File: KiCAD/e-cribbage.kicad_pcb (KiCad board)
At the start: 2 copper layers, 304.8 x 100.3 mm, 568 parts, among them U1 74HC595D_118, U10 74HC595D_118, U11 74HC595D_118, U12 74HC595D_118, U13 74HC595D_118, U14 74HC595D_118, U15 74HC595D_118, U16 74HC595D_118, U17 74HC595D_118, U18 74HC595D_118, U19 74HC595D_118, U2 MSP430F2012IPW, U20 74HC595D_118, U21 74HC595D_118, U22 74HC595D_118, U23 74HC595D_118, U24 74HC595D_118, U25 74HC595D_118, U26 74HC595D_118, U27 74HC595D_118, U28 74HC595D_118, U29 74HC595D_118, U3 74HC595D_118, U30 74HC595D_118, U31 74HC595D_118, U32 SN74LVC1G08DBVR, U34 SN74LVC1G08DBVR, U35 SN74LVC1G08DBVR, U36 SN74LVC1G08DBVR, U37 SN74LVC1G08DBVR, U38 SN74LVC1G08DBVR, U39 SN74LVC1G08DBVR, U4 74HC595D_118, U40 SN74LVC1G08DBVR, U5 74HC595D_118, U6 74HC595D_118, U7 74HC595D_118, U8 74HC595D_118, U9 74HC595D_118

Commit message: clock fanout added to schematic
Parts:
- moved C39 99.0 mm to (236.5, 172.0), turned to 270 degrees
- moved C38 96.8 mm to (222.2, 171.7), turned to 270 degrees
- moved C37 84.2 mm to (204.5, 172.0), turned to 270 degrees
- moved C36 74.5 mm to (189.5, 171.7), turned to 270 degrees
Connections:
- U10 pad 10: (no net) -> +3V3
- U10 pad 11: (no net) -> CLK1C
- U10 pad 12: (no net) -> CLK1C
- U10 pad 13: (no net) -> +3V3
- U11 pad 10: (no net) -> +3V3
- U11 pad 11: (no net) -> CLK1C
- U11 pad 12: (no net) -> CLK1C
- U11 pad 13: (no net) -> +3V3
- U12 pad 10: (no net) -> +3V3
- U12 pad 11: (no net) -> CLK1C
- U12 pad 12: (no net) -> CLK1C
- U12 pad 13: (no net) -> +3V3
- U13 pad 10: (no net) -> +3V3
- U13 pad 11: (no net) -> CLK1C
- U13 pad 12: (no net) -> CLK1C
- U13 pad 13: (no net) -> +3V3
- U14 pad 10: (no net) -> +3V3
- U14 pad 11: (no net) -> CLK1D
- U14 pad 12: (no net) -> CLK1D
- U14 pad 13: (no net) -> +3V3
- U15 pad 11: (no net) -> CLK1D
- U15 pad 12: (no net) -> CLK1D
- U16 pad 11: (no net) -> CLK1D
- U16 pad 12: (no net) -> CLK1D
- U16 pad 9: (no net) -> Net-(U16-Pad9)
- U17 pad 10: (no net) -> +3V3
- U17 pad 11: CLK -> CLK2A
- U17 pad 12: CLK -> CLK2A
- U17 pad 13: (no net) -> +3V3
- U18 pad 10: (no net) -> +3V3
- U18 pad 11: (no net) -> CLK2A
- U18 pad 12: (no net) -> CLK2A
- U18 pad 13: (no net) -> +3V3
- U18 pad 9: (no net) -> Net-(U18-Pad9)
- U19 pad 10: (no net) -> +3V3
- U19 pad 11: (no net) -> CLK2A
- U19 pad 12: (no net) -> CLK2A
- U19 pad 13: (no net) -> +3V3
- U19 pad 14: (no net) -> Net-(U19-Pad14)
- U2 pad 11: (no net) -> TEST
- U2 pad 6: (no net) -> Net-(U2-Pad6)
- U2 pad 9: (no net) -> Net-(U2-Pad9)
- U20 pad 10: (no net) -> +3V3
- U20 pad 11: (no net) -> CLK2A
- U20 pad 12: (no net) -> CLK2A
- U20 pad 13: (no net) -> +3V3
- U21 pad 10: (no net) -> +3V3
- U21 pad 11: (no net) -> CLK2B
- U21 pad 12: (no net) -> CLK2B
- U21 pad 13: (no net) -> +3V3
- U22 pad 10: (no net) -> +3V3
- U22 pad 11: (no net) -> CLK2B
- U22 pad 12: (no net) -> CLK2B
- U22 pad 13: (no net) -> +3V3
- U23 pad 10: (no net) -> +3V3
- U23 pad 11: (no net) -> CLK2B
- U23 pad 12: (no net) -> CLK2B
- U23 pad 13: (no net) -> +3V3
- U23 pad 9: (no net) -> Net-(U23-Pad9)
- U24 pad 10: (no net) -> +3V3
- U24 pad 11: (no net) -> CLK2B
- U24 pad 12: (no net) -> CLK2B
- U24 pad 13: (no net) -> +3V3
- U24 pad 14: (no net) -> Net-(U24-Pad14)
- U25 pad 10: (no net) -> +3V3
- U25 pad 11: (no net) -> Net-(U25-Pad11)
- U25 pad 12: (no net) -> Net-(U25-Pad12)
- U25 pad 13: (no net) -> +3V3
- U26 pad 10: (no net) -> +3V3
- U26 pad 11: (no net) -> CLK2C
- U26 pad 12: (no net) -> CLK2C
- U26 pad 13: (no net) -> +3V3
- U27 pad 10: (no net) -> +3V3
- U27 pad 11: (no net) -> CLK2C
- U27 pad 12: (no net) -> CLK2C
- U27 pad 13: (no net) -> +3V3
- U28 pad 10: (no net) -> +3V3
- U28 pad 11: (no net) -> CLK2C
- U28 pad 12: (no net) -> CLK2C
- U28 pad 13: (no net) -> +3V3
- U29 pad 10: (no net) -> +3V3
- U29 pad 11: (no net) -> CLK2D
- U29 pad 12: (no net) -> CLK2D
- U29 pad 13: (no net) -> +3V3
- U30 pad 10: (no net) -> +3V3
- U30 pad 11: (no net) -> CLK2D
- U30 pad 12: (no net) -> CLK2D
- U30 pad 13: (no net) -> +3V3
- U31 pad 10: (no net) -> +3V3
- U31 pad 11: (no net) -> CLK2D
- U31 pad 12: (no net) -> CLK2D
- U31 pad 13: (no net) -> +3V3
- U31 pad 9: (no net) -> Net-(U31-Pad9)
- U34 pad 4: (no net) -> CLK1B
- U35 pad 4: (no net) -> CLK1C
- U36 pad 4: (no net) -> CLK1D
- U37 pad 4: (no net) -> CLK2A
- U38 pad 4: (no net) -> CLK2B
- U39 pad 4: (no net) -> CLK2C
- U40 pad 4: (no net) -> CLK2D
- U5 pad 10: (no net) -> +3V3
- U5 pad 13: (no net) -> +3V3
- U6 pad 10: (no net) -> +3V3
- U6 pad 11: (no net) -> CLK1B
- U6 pad 12: (no net) -> CLK1B
- U6 pad 13: (no net) -> +3V3
- U7 pad 10: (no net) -> +3V3
- U7 pad 11: (no net) -> CLK1B
- U7 pad 12: (no net) -> CLK1B
- U7 pad 13: (no net) -> +3V3
- U7 pad 9: (no net) -> Net-(U7-Pad9)
- U8 pad 10: (no net) -> +3V3
- U8 pad 11: (no net) -> CLK1B
- U8 pad 12: (no net) -> CLK1B
- U8 pad 13: (no net) -> +3V3
- U8 pad 14: (no net) -> Net-(U8-Pad14)
- U9 pad 10: (no net) -> +3V3
- U9 pad 11: (no net) -> CLK1B
- U9 pad 12: (no net) -> CLK1B
- U9 pad 13: (no net) -> +3V3
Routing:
- net GND: track 594.2 -> 619.8 mm, vias 303 -> 307
- net CLK: track 141.6 -> 132.6 mm
- net +3V3: track 301.5 -> 308.2 mm, vias 53 -> 57

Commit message: OE pulled low
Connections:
- U1 pad 13: +3V3 -> GND
- U10 pad 13: +3V3 -> GND
- U11 pad 13: +3V3 -> GND
- U12 pad 13: +3V3 -> GND
- U13 pad 13: +3V3 -> GND
- U14 pad 13: +3V3 -> GND
- U15 pad 13: +3V3 -> GND
- U16 pad 13: +3V3 -> GND
- U17 pad 13: +3V3 -> GND
- U18 pad 13: +3V3 -> GND
- U19 pad 13: +3V3 -> GND
- U20 pad 13: +3V3 -> GND
- U21 pad 13: +3V3 -> GND
- U22 pad 13: +3V3 -> GND
- U25 pad 11: Net-(U25-Pad11) -> CLK2C
- U25 pad 12: Net-(U25-Pad12) -> CLK2C
- U25 pad 13: +3V3 -> GND
- U26 pad 13: +3V3 -> GND
- U27 pad 13: +3V3 -> GND
- U28 pad 13: +3V3 -> GND
- U29 pad 13: +3V3 -> GND
- U3 pad 13: +3V3 -> GND
- U30 pad 13: +3V3 -> GND
- U31 pad 13: +3V3 -> GND
- U5 pad 13: +3V3 -> GND
- U6 pad 13: +3V3 -> GND
- U7 pad 13: +3V3 -> GND
- U8 pad 13: +3V3 -> GND
- U9 pad 13: +3V3 -> GND
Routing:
- net +3V3: track 308.2 -> 303.6 mm

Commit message: added FET connector
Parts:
- added J1: Conn_01x04_Female, Connector_PinHeader_1.27mm:PinHeader_1x04_P1.27mm_Vertical, F.Cu at (134.2, 163.7)
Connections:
- net RST renamed Net-(J1-Pad3)
- U2 pad 11: TEST -> Net-(J1-Pad2)

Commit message: created local library
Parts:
- D1, D10, D100, D101, D102, D103, D104, D105, D106, D107, D108, D109, D11, D110, D111, D112, D113, D114, D115, D116, D117, D118, D119, D12, D120, D121, D122, D123, D124, D125, D126, D127, D128, D129, D13, D130, D131, D132, D133, D134, D135, D136, D137, D138, D139, D14, D140, D141, D142, D143, D144, D145, D146, D147, D148, D149, D15, D150, D151, D152, D153, D154, D155, D156, D157, D158, D159, D16, D160, D161, D162, D163, D164, D165, D166, D167, D168, D169, D17, D170, D171, D172, D173, D174, D175, D176, D177, D178, D179, D18, D180, D181, D182, D183, D184, D185, D186, D187, D188, D189, D19, D190, D191, D192, D193, D194, D195, D196, D197, D198, D199, D2, D20, D200, D201, D202, D203, D204, D205, D206, D207, D208, D209, D21, D210, D211, D212, D213, D214, D215, D216, D217, D218, D219, D22, D220, D221, D222, D223, D224, D225, D226, D227, D228, D229, D23, D230, D231, D232, D233, D234, D235, D236, D237, D238, D239, D24, D240, D25, D26, D27, D28, D29, D3, D30, D31, D32, D33, D34, D35, D36, D37, D38, D39, D4, D40, D41, D42, D43, D44, D45, D46, D47, D48, D49, D5, D50, D51, D52, D53, D54, D55, D56, D57, D58, D59, D6, D60, D61, D62, D63, D64, D65, D66, D67, D68, D69, D7, D70, D71, D72, D73, D74, D75, D76, D77, D78, D79, D8, D80, D81, D82, D83, D84, D85, D86, D87, D88, D89, D9, D90, D91, D92, D93, D94, D95, D96, D97, D98, D99: footprint LEDs:LED_0603 -> e-cribbage:LED_0603
- R1, R10, R100, R101, R102, R103, R104, R105, R106, R107, R108, R109, R11, R110, R111, R112, R113, R114, R115, R116, R117, R118, R119, R12, R120, R121, R122, R123, R124, R125, R126, R127, R128, R129, R13, R130, R131, R132, R133, R134, R135, R136, R137, R138, R139, R14, R140, R141, R142, R143, R144, R145, R146, R147, R148, R149, R15, R150, R151, R152, R153, R154, R155, R156, R157, R158, R159, R16, R160, R161, R162, R163, R164, R165, R166, R167, R168, R169, R17, R170, R171, R172, R173, R174, R175, R176, R177, R178, R179, R18, R180, R181, R182, R183, R184, R185, R186, R187, R188, R189, R19, R190, R191, R192, R193, R194, R195, R196, R197, R198, R199, R2, R20, R200, R201, R202, R203, R204, R205, R206, R207, R208, R209, R21, R210, R211, R212, R213, R214, R215, R216, R217, R218, R219, R22, R220, R221, R222, R223, R224, R225, R226, R227, R228, R229, R23, R230, R231, R232, R233, R234, R235, R236, R237, R238, R239, R24, R240, R243, R244, R246, R247, R25, R251, R26, R27, R28, R29, R3, R30, R31, R32, R33, R34, R35, R36, R37, R38, R39, R4, R40, R41, R42, R43, R44, R45, R46, R47, R48, R49, R5, R50, R51, R52, R53, R54, R55, R56, R57, R58, R59, R6, R60, R61, R62, R63, R64, R65, R66, R67, R68, R69, R7, R70, R71, R72, R73, R74, R75, R76, R77, R78, R79, R8, R80, R81, R82, R83, R84, R85, R86, R87, R88, R89, R9, R90, R91, R92, R93, R94, R95, R96, R97, R98, R99: footprint Resistors_SMD:R_0603 -> e-cribbage:R_0603

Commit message: schematic fixes + routes + battery clip
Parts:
- moved C21 0.66 mm to (347.6, 97.0)
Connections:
- U23 pad 13: +3V3 -> GND
- U24 pad 13: +3V3 -> GND
- U4 pad 13: +3V3 -> GND
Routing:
- net GND: track 619.8 -> 800.5 mm, vias 307 -> 320
- net +3V3: track 303.6 -> 430.7 mm, vias 57 -> 71
- net Net-(D161-Pad2): track 0.00 -> 28.5 mm
- net CLK1A: track 81.3 -> 73.7 mm
- net Net-(D49-Pad2): track 0.00 -> 7.63 mm
- net Net-(U30-Pad9): track 161.3 -> 158.3 mm
- net CLK2A: track 0.00 -> 2.60 mm
- net CLK1B: track 0.00 -> 2.60 mm
- net CLK2B: track 0.00 -> 2.60 mm
- net Net-(U14-Pad9): track 70.8 -> 69.2 mm
- net Net-(D25-Pad2): track 21.6 -> 20.3 mm
- net Net-(D127-Pad2): track 12.0 -> 10.9 mm
- net Net-(D162-Pad2): track 27.1 -> 28.0 mm

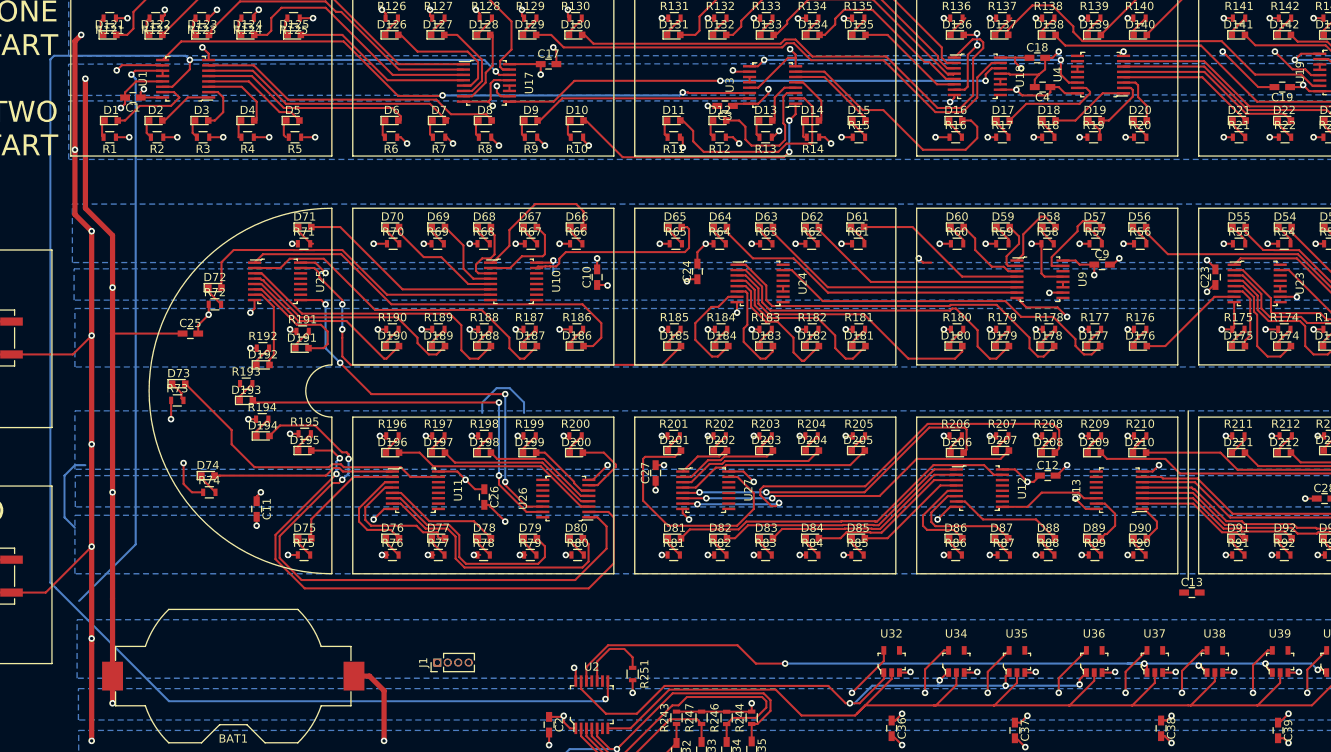
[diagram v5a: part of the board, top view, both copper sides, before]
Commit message: clock routing
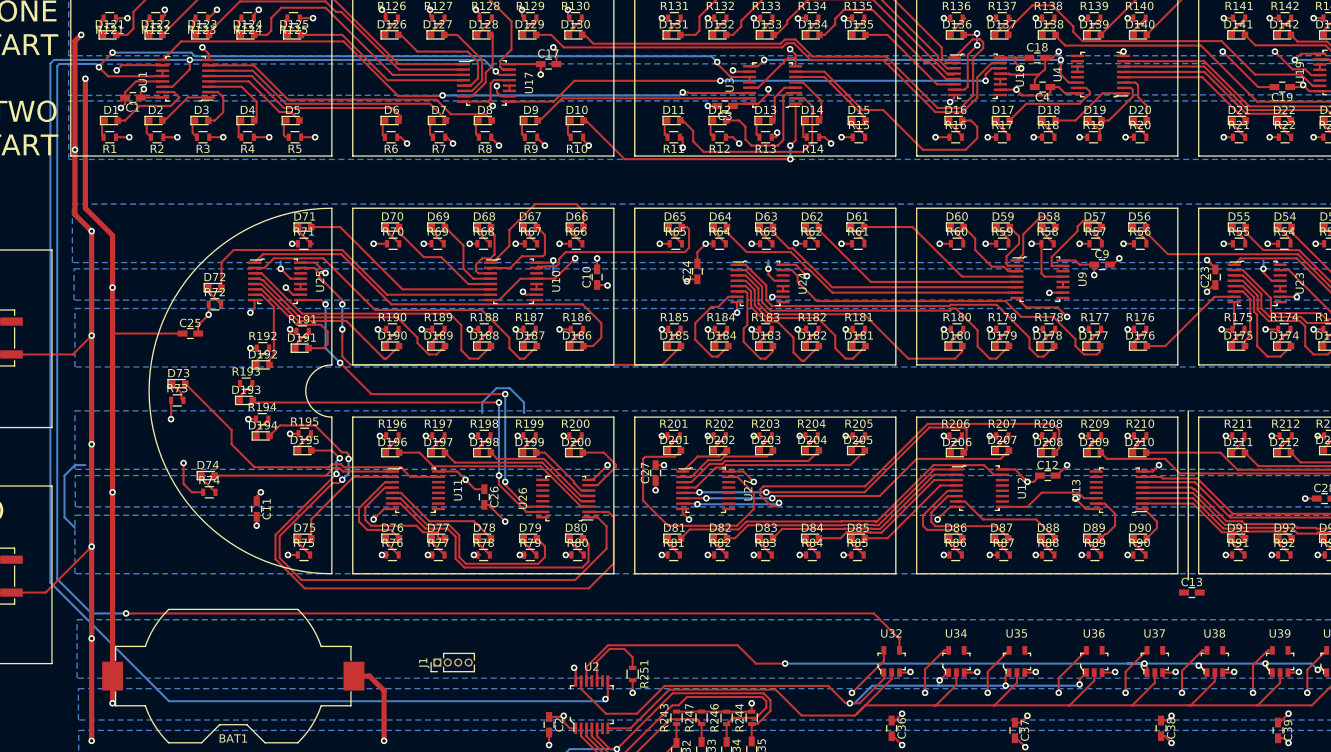
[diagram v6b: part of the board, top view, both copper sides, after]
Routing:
- net CLK1A: track 73.7 -> 266.6 mm, vias 1 -> 4
- net GND: track 800.5 -> 822.6 mm, vias 320 -> 323
- net +3V3: track 430.7 -> 439.4 mm, vias 71 -> 75
- net Net-(D177-Pad2): track 43.7 -> 44.5 mm
- net Net-(D10-Pad2): track 33.0 -> 33.8 mm
- net DATA: track 201.8 -> 201.1 mm
- net CLK2C: track 0.00 -> 0.65 mm
- net CLK1C: track 0.00 -> 0.65 mm

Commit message: schematic fix + more clock routes
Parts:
- moved C13 19.1 mm to (209.8, 145.1), turned to 270 degrees
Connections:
- U16 pad 9: Net-(U16-Pad9) -> (no net)
- U19 pad 14: Net-(U19-Pad14) -> Net-(U18-Pad9)
- U2 pad 6: Net-(U2-Pad6) -> (no net)
- U2 pad 9: Net-(U2-Pad9) -> (no net)
- U23 pad 9: Net-(U23-Pad9) -> (no net)
- U24 pad 14: Net-(U24-Pad14) -> (no net)
- U31 pad 9: Net-(U31-Pad9) -> (no net)
- U7 pad 9: Net-(U7-Pad9) -> (no net)
- U8 pad 14: Net-(U8-Pad14) -> (no net)
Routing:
- net CLK2A: track 2.60 -> 325.4 mm, vias 0 -> 4
- net CLK1B: track 2.60 -> 281.6 mm, vias 0 -> 1
- net CLK2C: track 0.65 -> 182.7 mm, vias 0 -> 2
- net CLK1D: track 0.00 -> 126.7 mm, vias 0 -> 3
- net CLK1A: track 266.6 -> 378.6 mm, vias 4 -> 6
- net CLK2B: track 2.60 -> 114.2 mm, vias 0 -> 4
- net Net-(U4-Pad9): track 0.00 -> 99.8 mm, vias 0 -> 2
- net Net-(U5-Pad9): track 0.00 -> 99.6 mm, vias 0 -> 4
- net GND: track 822.6 -> 912.2 mm, vias 323 -> 328
- net CLK2D: track 0.00 -> 44.9 mm, vias 0 -> 2
- net Net-(U18-Pad9): track 0.00 -> 44.1 mm, vias 0 -> 2
- net +3V3: track 439.4 -> 483.0 mm, vias 75 -> 85
- net Net-(U26-Pad9): track 0.00 -> 26.2 mm, vias 0 -> 2
- net Net-(J1-Pad2): track 0.00 -> 21.0 mm, vias 0 -> 2
- net Net-(J1-Pad3): track 9.03 -> 27.9 mm, vias 0 -> 2
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
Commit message: more clock routes
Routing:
- net CLK2D: track 44.9 -> 220.0 mm, vias 2 -> 3
- net CLK2C: track 182.7 -> 244.9 mm
- net CLK1D: track 126.7 -> 169.6 mm, vias 3 -> 4
- net CLK1C: track 14.2 -> 44.0 mm, vias 0 -> 2
- net GND: track 912.2 -> 924.7 mm, vias 328 -> 332
- net +3V3: track 483.0 -> 491.4 mm, vias 85 -> 87
- net Net-(C32-Pad1): track 182.5 -> 187.8 mm
- net Net-(C34-Pad1): track 168.4 -> 173.3 mm
- net Net-(C33-Pad1): track 209.7 -> 212.3 mm
- net Net-(D97-Pad2): track 62.4 -> 64.3 mm
- net Net-(C35-Pad1): track 187.0 -> 188.6 mm
- net Net-(D114-Pad2): track 8.18 -> 7.12 mm
- net Net-(D225-Pad2): track 22.9 -> 23.6 mm
- net Net-(D221-Pad2): track 20.9 -> 21.4 mm
- net CLK2A: track 325.4 -> 325.9 mm
